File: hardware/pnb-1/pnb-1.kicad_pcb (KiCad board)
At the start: 2 copper layers, 58 x 42 mm, 37 parts, among them J1 USB-C 16P, J3 DTR 2x6, J4 UART 1x4, SW1 BOOT, SW2 RESET, U1 ESP32-S3-MINI-1-N8, U2 AMS1117-3.3, U3 SCD41-D-R2, U4 BH1750FVI-TR

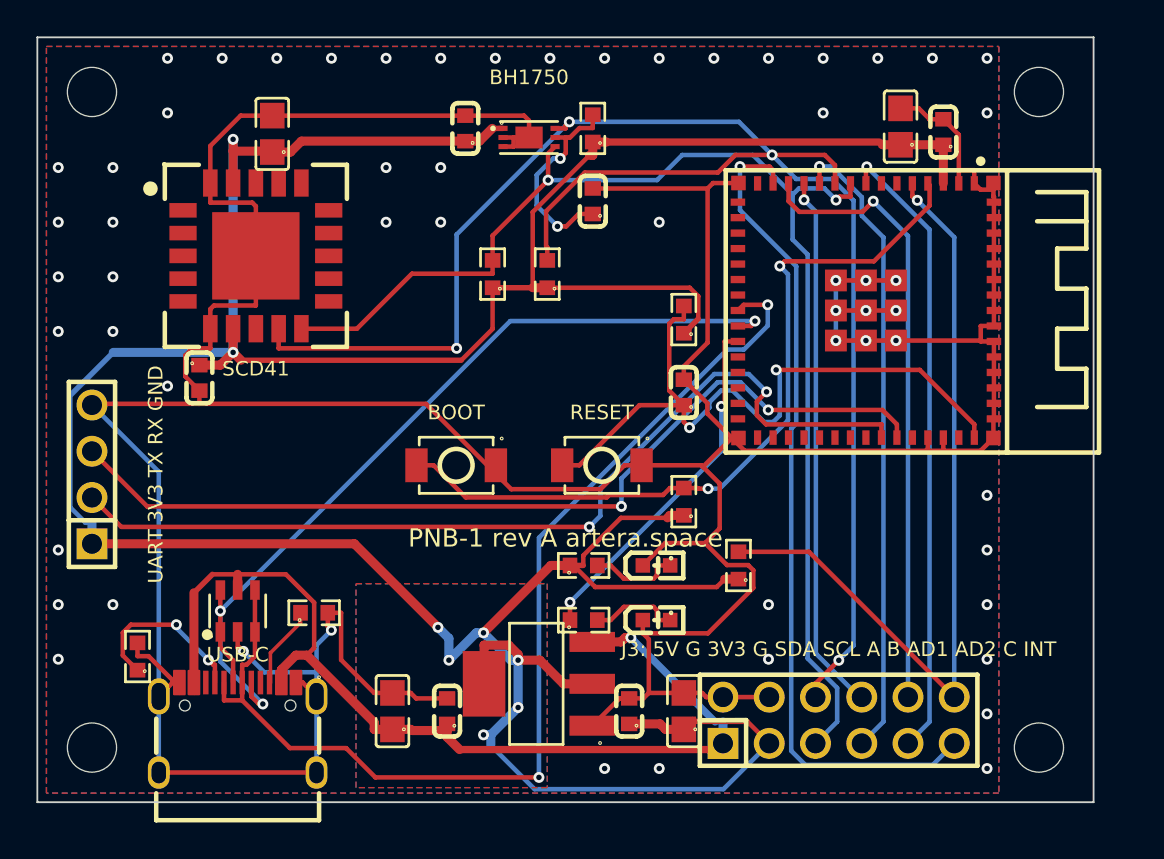
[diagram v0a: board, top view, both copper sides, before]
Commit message: feat(pcb): validate an order-ready sensor board
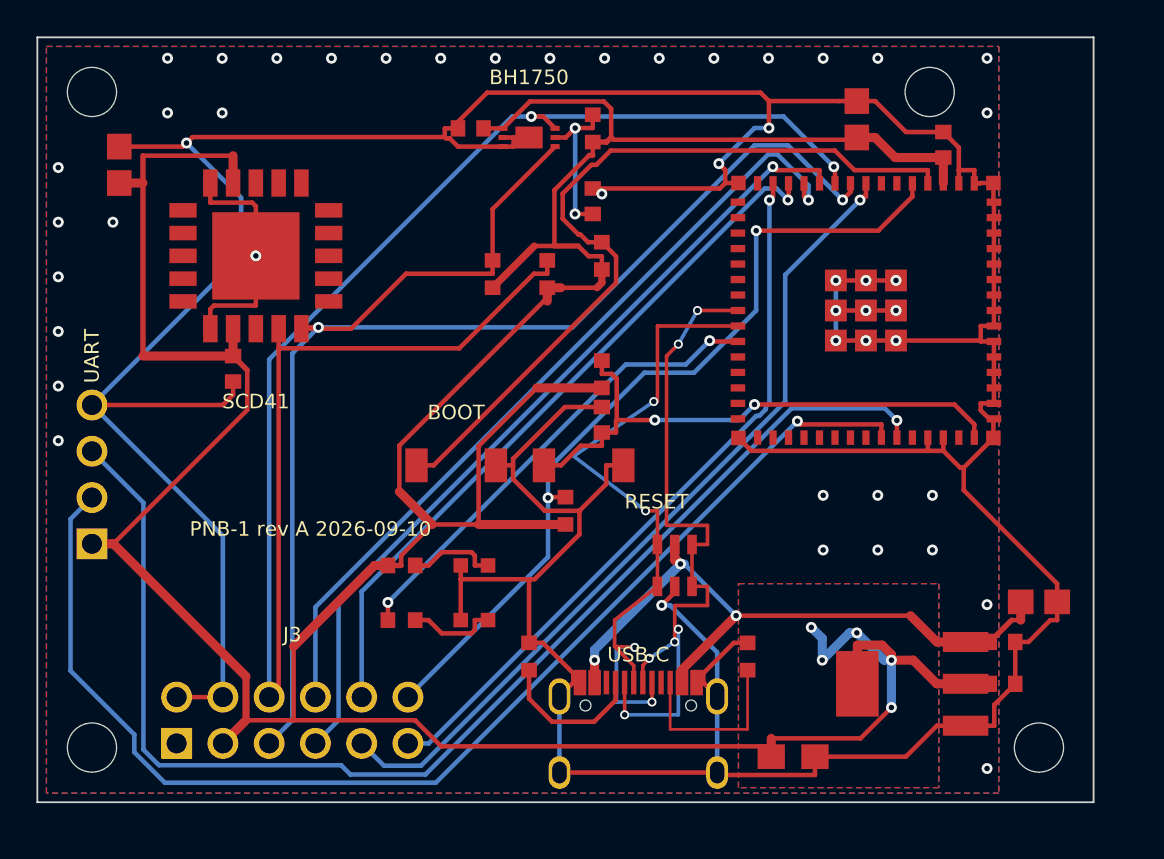
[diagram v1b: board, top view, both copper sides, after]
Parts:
- C9: value 22uF -> 22uF tantalum; footprint C0805 -> CASE-A_3216
- moved C8 36.0 mm to (55.0, 31.0), turned to 0 degrees
- moved C2 30.7 mm to (53.0, 33.2), turned to 0 degrees
- moved J3 30.0 mm to (14.0, 37.5)
- moved D1 24.1 mm to (35.0, 29.0)
- moved R4 23.9 mm to (39.0, 34.0), turned to 90 degrees
- moved J1 22.0 mm to (33.0, 37.9)
- moved R3 21.5 mm to (27.0, 34.0)
- moved C3 20.6 mm to (53.0, 35.5), turned to 0 degrees
- moved U2 20.5 mm to (48.0, 35.5)
- moved R2 14.2 mm to (31.0, 12.0)
- moved LED1 10.0 mm to (24.0, 29.0)
- moved LED2 10.0 mm to (24.0, 32.0)
- moved R8 10.0 mm to (20.0, 29.0)
- moved R9 10.0 mm to (20.0, 32.0)
- moved R10 9.96 mm to (29.0, 26.0)
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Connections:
- J3 pad 1: VBUS -> (no net)
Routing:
- net GND: track 260.2 -> 290.5 mm, vias 58 -> 48
- net USB_DN: track 60.0 -> 39.5 mm, vias 2 -> 6
- net VBUS: track 55.3 -> 36.6 mm, vias 1 -> 3
- net RXD0: track 50.9 -> 69.0 mm, vias 2 -> 1
- net DTR_GPIOB: track 29.6 -> 44.9 mm
- net TXD0: track 51.8 -> 66.7 mm, vias 2 -> 1
- net DTR_ADCA: track 34.5 -> 45.9 mm
- net USB_DP: track 50.0 -> 38.8 mm, vias 3 -> 4
- net DTR_GPIOA: track 34.9 -> 45.4 mm
- net SDA: track 71.1 -> 80.3 mm
- net EN: track 38.1 -> 30.9 mm
- net 3V3: track 206.2 -> 213.3 mm, vias 8 -> 5
- net IO21: track 19.5 -> 26.2 mm
- net DTR_GPIOC: track 45.9 -> 39.8 mm
- net CC2: track 4.51 -> 10.1 mm
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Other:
- board text added: "J3"
- board text added: "PNB-1 rev A 2026-09-10"
- board text added: "UART"
- board text removed: "J3: 5V G 3V3 G SDA SCL A B AD1 AD2 C INT"
- board text removed: "PNB-1 rev A artera.space"
- board text removed: "UART 3V3 TX RX GND"

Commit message: fix(pcb): correct sensor land pattern and release gates
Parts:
- J3: value DTR 2x6 -> DTR 2x6 DNP
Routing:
- net GND: track 290.5 -> 235.0 mm, vias 48 -> 53
- net SCL: track 96.4 -> 116.3 mm
- net USB_DP: track 38.8 -> 38.0 mm
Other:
- board text added: "+"
- board text added: "J3 DNP"
- board text removed: "J3"
